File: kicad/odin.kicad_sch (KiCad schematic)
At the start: 0 parts

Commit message: Islands, city plan, HDMI out and the eight-layer stackup
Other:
- added sheet Video (video.kicad_sch)
- note added: "Video: HDMI out from bank 35 (TMDS_33) through a TPD12S016"
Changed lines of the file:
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@@
 	)
 	(text "Network: RTL8211FD-CG gigabit PHY and ETH jack, LINK P and LINK Q raw LVDS ports" (at 273 127 0) (effects (font (size 2 2)) (justify left)))
+	(sheet (at 30 175) (size 95 40)
+		(stroke (width 0.1524) (type solid)) (fill (color 0 0 0 0.0000))
+		(property "Sheetname" "Video" (at 30 174 0) (effects (font (size 2.5 2.5)) (justify left bottom)))
+		(property "Sheetfile" "video.kicad_sch" (at 30 216 0) (effects (font (size 2 2)) (justify left top)))
+		(instances (project "odin" (path "/c44fb7fe-6133-ad34-68fd-fb66126197ef" (page "8"))))
+	)
+	(text "Video: HDMI out from bank 35 (TMDS_33) through a TPD12S016" (at 33 187 0) (effects (font (size 2 2)) (justify left)))
 	(sheet_instances (path "/" (page "1")))
 )

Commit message: Step 4: SDRAM
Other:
- note added: "PSRAM x4 (independent buses, 1.8 V), SDRAM and configuration flash"
- note removed: "PSRAM x4 (independent buses) and configuration flash"
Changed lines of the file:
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@@
 		(instances (project "odin" (path "/c44fb7fe-6133-ad34-68fd-fb66126197ef" (page "4"))))
 	)
-	(text "PSRAM x4 (independent buses) and configuration flash" (at 273 67 0) (effects (font (size 2 2)) (justify left)))
+	(text "PSRAM x4 (independent buses, 1.8 V), SDRAM and configuration flash" (at 273 67 0) (effects (font (size 2 2)) (justify left)))
 	(sheet (at 30 115) (size 95 40)
 		(stroke (width 0.1524) (type solid)) (fill (color 0 0 0 0.0000))

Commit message: Step 5: MRAM, optional populate
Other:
- note added: "PSRAM x4 (independent buses, 1.8 V), SDRAM, MRAM option and configuration flash"
- note removed: "PSRAM x4 (independent buses, 1.8 V), SDRAM and configuration flash"
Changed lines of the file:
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@@
 		(instances (project "odin" (path "/c44fb7fe-6133-ad34-68fd-fb66126197ef" (page "4"))))
 	)
-	(text "PSRAM x4 (independent buses, 1.8 V), SDRAM and configuration flash" (at 273 67 0) (effects (font (size 2 2)) (justify left)))
+	(text "PSRAM x4 (independent buses, 1.8 V), SDRAM, MRAM option and configuration flash" (at 273 67 0) (effects (font (size 2 2)) (justify left)))
 	(sheet (at 30 115) (size 95 40)
 		(stroke (width 0.1524) (type solid)) (fill (color 0 0 0 0.0000))

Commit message: Step 6: microSD socket
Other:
- note added: "PSRAM x4 (independent buses, 1.8 V), SDRAM, MRAM option, microSD and configuration flash"
- note removed: "PSRAM x4 (independent buses, 1.8 V), SDRAM, MRAM option and configuration flash"
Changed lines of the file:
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@@
 		(instances (project "odin" (path "/c44fb7fe-6133-ad34-68fd-fb66126197ef" (page "4"))))
 	)
-	(text "PSRAM x4 (independent buses, 1.8 V), SDRAM, MRAM option and configuration flash" (at 273 67 0) (effects (font (size 2 2)) (justify left)))
+	(text "PSRAM x4 (independent buses, 1.8 V), SDRAM, MRAM option, microSD and configuration flash" (at 273 67 0) (effects (font (size 2 2)) (justify left)))
 	(sheet (at 30 115) (size 95 40)
 		(stroke (width 0.1524) (type solid)) (fill (color 0 0 0 0.0000))

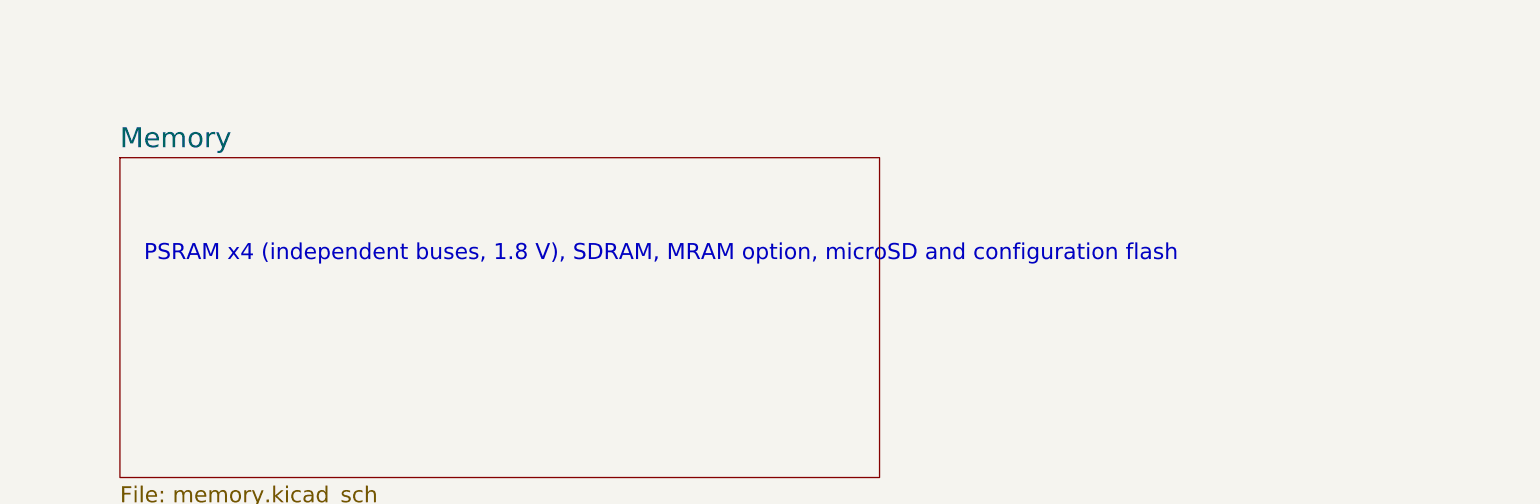
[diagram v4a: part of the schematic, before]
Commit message: MRAM fitted on every board
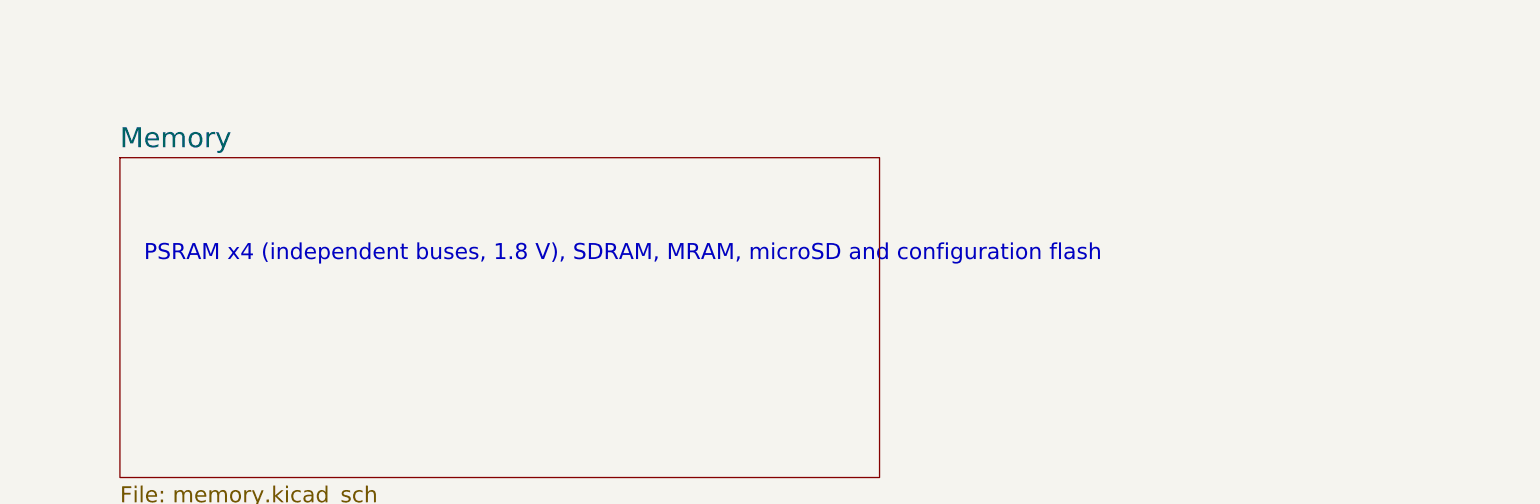
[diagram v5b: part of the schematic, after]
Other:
- note added: "PSRAM x4 (independent buses, 1.8 V), SDRAM, MRAM, microSD and configuration flash"
- note removed: "PSRAM x4 (independent buses, 1.8 V), SDRAM, MRAM option, microSD and configuration flash"
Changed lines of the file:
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@@
 		(instances (project "odin" (path "/c44fb7fe-6133-ad34-68fd-fb66126197ef" (page "4"))))
 	)
-	(text "PSRAM x4 (independent buses, 1.8 V), SDRAM, MRAM option, microSD and configuration flash" (at 273 67 0) (effects (font (size 2 2)) (justify left)))
+	(text "PSRAM x4 (independent buses, 1.8 V), SDRAM, MRAM, microSD and configuration flash" (at 273 67 0) (effects (font (size 2 2)) (justify left)))
 	(sheet (at 30 115) (size 95 40)
 		(stroke (width 0.1524) (type solid)) (fill (color 0 0 0 0.0000))
